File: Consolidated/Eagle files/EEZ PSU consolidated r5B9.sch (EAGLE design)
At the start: 534 parts, among them IC1 LTC3864EMSE#PBF, IC10 REF5025AIDG4, IC11 DAC8552IDGKTG4, IC12 ADG465SOT-23, IC13 TS5A9411DCKT, IC14 ADS1120IPWR, IC15 LP339D, IC16 LM25575MH/NOPB, IC17 TPD4E002DRLR, IC18 TPD2E001DZDR, IC19 ADUM3160BRWZ, IC2 MC79L05, IC20 TLC5925IDBQR, IC21 Si8641EC-B-IS1, IC22 SI8651EC-B-IS1, IC23 SI8651EC-B-IS1, IC24 LD1117ADT33TR, IC25 Si8641EC-B-IS1, IC26 PCA21125T/Q900/1,1, IC27 AT25256B-SSHL-B, IC28 W5500, IC29 BC857BS, IC3 MC78L05, IC30 TLC555, IC31 SN74LVC2G08DCTR, IC32 TPS3705-33D, IC33 SN74LV1T34DBVR, IC34 SN74LVC2G02DCTR, IC4 LM5574MTX/NOPB, IC5 LP2951SO8, IC6 TL072D, IC7 TL072D, IC8 OP27GSZ, IC9 MCP23S08-E/SO, J1 BS-244DSM-R, J2 BS-244DSM-G, J3 BS-244DSM-B, J4 BS-244DSM-R, J5 BS-244DSM-B, Q1 IRFR5305, Q10 MMBT5401, Q11 MMBT5401, Q12 MMBT5551, Q13 MMBT5551, Q14 BSS84P, Q15 2N7002, Q16 MMBT5551, Q17 MMBT5401, Q18 MMBT5551, Q19 MMBT5551, Q2 MMBT5401, Q20 BTA26-600, Q21 BTA26-600, Q22 IRLL014N, Q23 IRLML2246TRPBF, Q24 IRLML2246TRPBF, Q25 IRLML2246TRPBF, Q26 IRLML2246TRPBF, Q27 2N7002, Q28 IRLML2246TRPBF, Q29 2N7002, Q3 2N7002, Q30 2N7002, Q4 IRFP250N, Q5 BC857C, Q6 BC846C, Q7 BCP56-16.115, Q8 IRFR5410, Q9 BCP56-16.115, SW1 A101SYCQ04, SW2 1301.9316, X1 39303035, X10 826629-5, X11 2411-01, X12 MC000006, X13 TSW-113-07-F-D, X14 MC000005, X15 TSW-113-07-F-D, X16 09185067324, X17 22-23-2021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

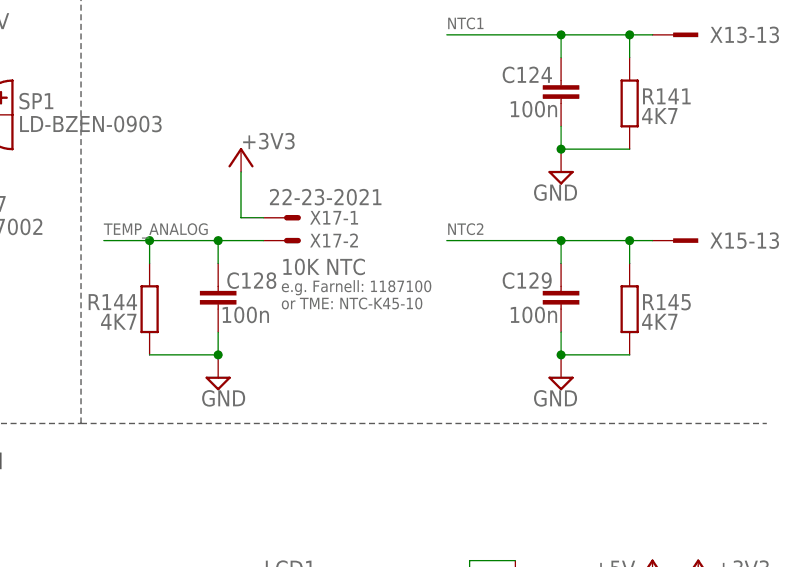
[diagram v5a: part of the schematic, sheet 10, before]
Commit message: NTC values updated
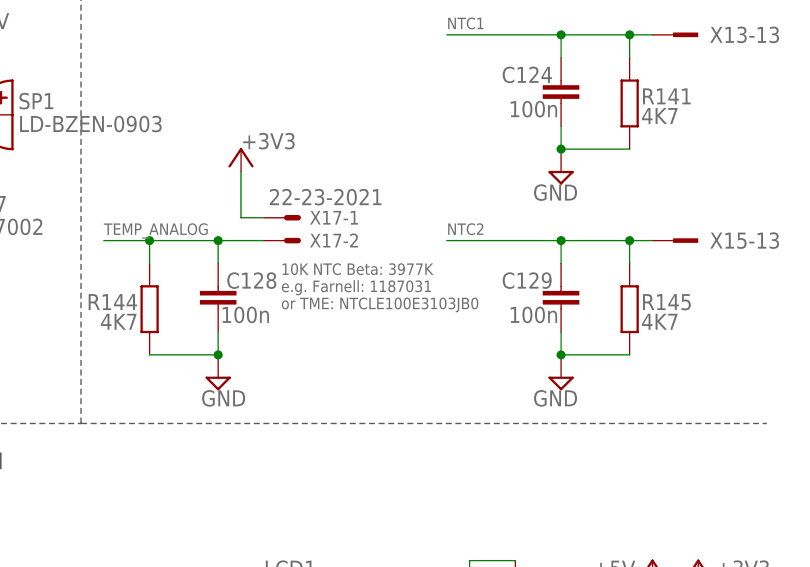
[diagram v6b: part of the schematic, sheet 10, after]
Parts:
- NTC1: value 10K/Beta:3570K -> NTCS0805E3103JMT
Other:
- note added: "10K NTC Beta: 3570K"
- note added: "10K NTC Beta: 3977K"
- note added: "e.g. Farnell: 1187031"
- note added: "or TME: NTCLE100E3103JB0"
- note removed: "10K NTC"
- note removed: "e.g. Farnell: 1187100"
- note removed: "or TME: NTC-K45-10"
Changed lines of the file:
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@@
 <setting verticaltext="up"/>
 </settings>
-<grid distance="0.1" unitdist="inch" unit="inch" style="lines" multiple="1" display="no" altdistance="0.01" altunitdist="inch" altunit="inch"/>
+<grid distance="0.025" unitdist="inch" unit="inch" style="lines" multiple="1" display="no" altdistance="0.01" altunitdist="inch" altunit="inch"/>
 <layers>
 <layer number="1" name="Top" color="4" fill="1" visible="no" active="no"/>
@@
 <part name="P+14" library="supply1" deviceset="+5V" device=""/>
 <part name="R103" library="rcl" deviceset="R-EU_" device="R0805" value="47K"/>
-<part name="NTC1" library="EEZ_Lib1" deviceset="NTC" device="0805" value="10K/Beta:3570K"/>
+<part name="NTC1" library="EEZ_Lib1" deviceset="NTC" device="0805" value="NTCS0805E3103JMT"/>
 <part name="P+15" library="supply2" deviceset="V+" device=""/>
 <part name="P+4" library="supply2" deviceset="V+" device=""/>
@@
 <wire x1="246.38" y1="-64.135" x2="233.68" y2="-64.135" width="0.1524" layer="103"/>
 <wire x1="223.52" y1="-64.135" x2="233.68" y2="-64.135" width="0.1524" layer="103"/>
+<text x="350.52" y="-86.36" size="1.27" layer="96">10K NTC Beta: 3570K</text>
 </plain>
 <instances>
@@
 <plain>
 <text x="164.465" y="29.845" size="2.54" layer="94" font="vector">TFT-touchscreen, RTC, EEPROM, Ethernet</text>
-<text x="207.645" y="141.605" size="1.27" layer="96">e.g. Farnell: 1187100</text>
-<text x="207.645" y="143.51" size="1.778" layer="96">10K NTC</text>
-<text x="207.645" y="139.7" size="1.27" layer="96">or TME: NTC-K45-10</text>
+<text x="207.645" y="141.605" size="1.27" layer="96">e.g. Farnell: 1187031</text>
+<text x="207.645" y="143.51" size="1.27" layer="96">10K NTC Beta: 3977K</text>
+<text x="207.645" y="139.7" size="1.27" layer="96">or TME: NTCLE100E3103JB0</text>
 <text x="164.465" y="26.035" size="2.54" layer="94" font="vector">Buzzer, temperature sensor (NTC)</text>
 <polygon width="0.1524" layer="91">
